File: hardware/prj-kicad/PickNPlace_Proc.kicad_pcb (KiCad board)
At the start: 4 copper layers, 200 x 90 mm, 110 parts, among them J1 Conn_01x09, J10 Conn_01x05, J11 Conn_02x05_Odd_Even, J12 Conn_02x05_Odd_Even, J13 Conn_01x05, J14 Conn_01x03, J15 Conn_01x06, J16 Conn_01x06, J17 Conn_01x12, J2 Conn_01x04, J3 Conn_01x06, J4 Conn_01x04, J5 Conn_01x06, J6 Conn_01x09, J7 Conn_01x02, J8 Conn_01x02, J9 Conn_01x06, Q1 Q_NPN, Q2 Q_NPN, SW1 SW_PUSH, U1 STM32F745ZX, U10 TXS0108E-RGY, U11 TXS0108E-RGY, U2 LM1117-5.0, U3 TPS54160A, U4 TPS54160A, U5 LM1117-5.0, U6 MCP6001T-I_OT, U7 MCP6001T-I_OT, U8 MCP6001T-I_OT, U9 MCP6001T-I_OT

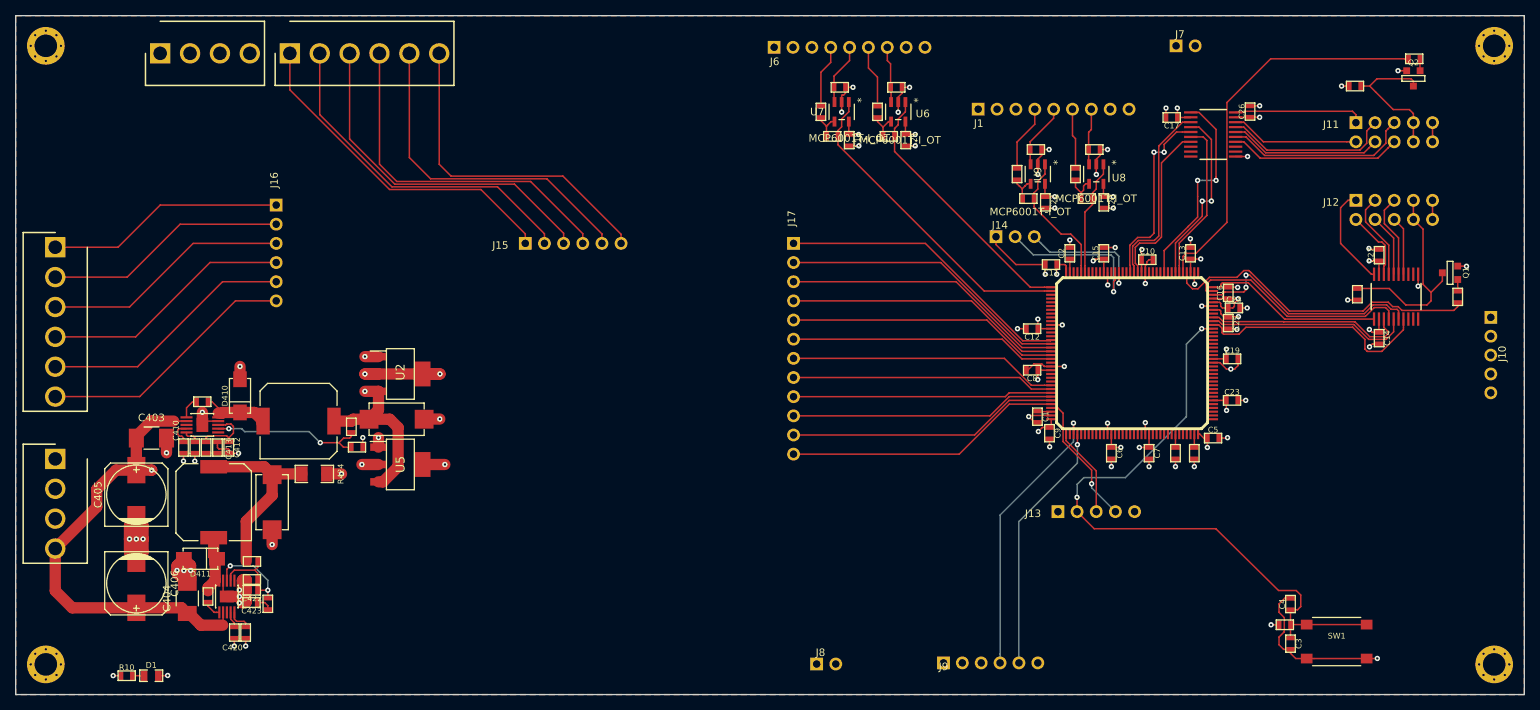
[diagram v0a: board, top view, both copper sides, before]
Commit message: Hardware update (rev2) Pumps, valve, pressure sensors, light, needle + fix enable on lvl shifter
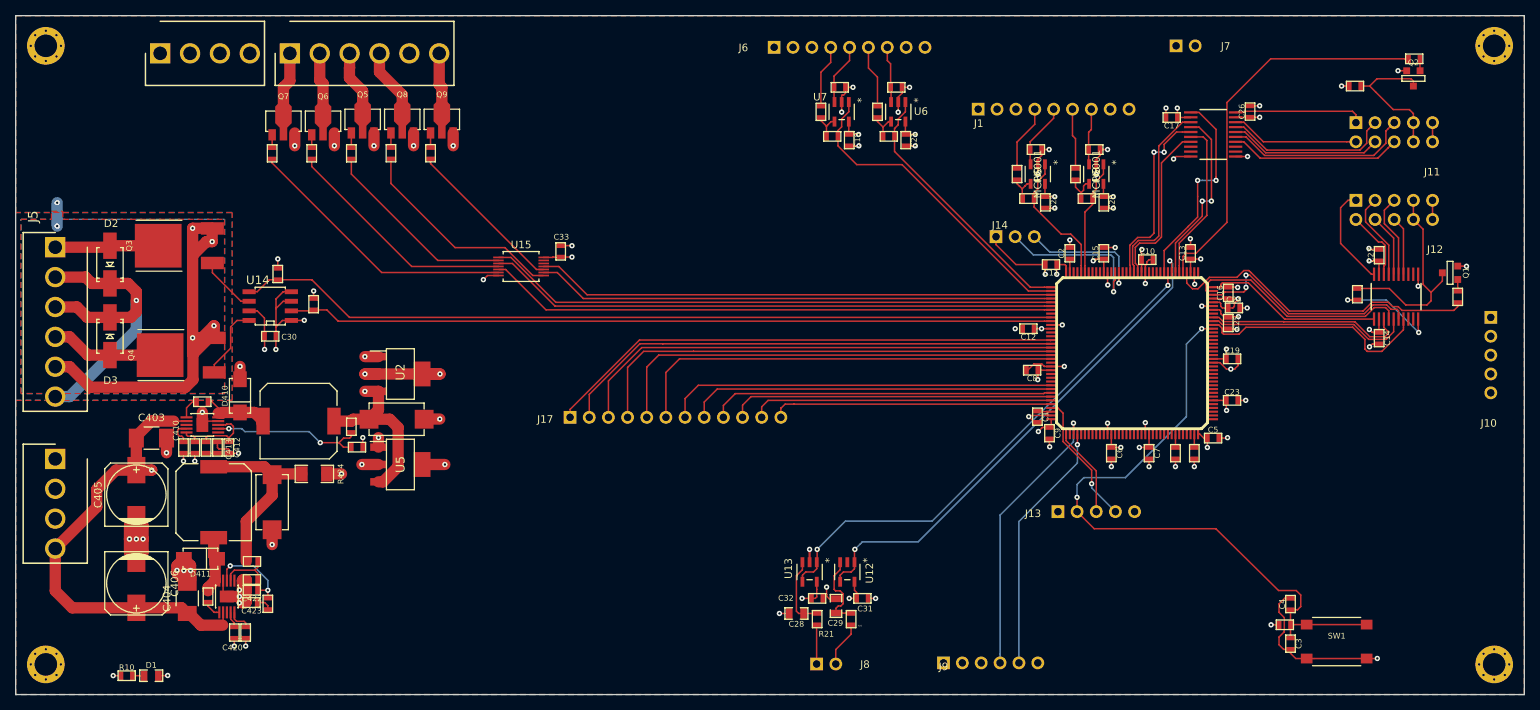
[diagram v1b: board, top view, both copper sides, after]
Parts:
- removed J15, J16: Conn_01x06, PickAndPlace:2_54____6pins
- added C28: 1uF, PickAndPlace:SMD0805, F.Cu at (152.0, 139.2)
- added C29: 1uF, PickAndPlace:SMD0805, F.Cu at (157.2, 138.2)
- added C30: 1uF, PickAndPlace:SMD0603, F.Cu at (82.2, 102.5)
- added C31: 100nF, PickAndPlace:SMD0603, F.Cu at (160.8, 137.2)
- added C32: 100nF, PickAndPlace:SMD0603, F.Cu at (154.8, 137.2)
- added C33: 100nF, PickAndPlace:SMD0603, F.Cu at (120.8, 91.2)
- added D2: S1MLR3, PickAndPlace:D_SMA, F.Cu at (61.0, 93.0)
- added D3: S1MLR3, PickAndPlace:D_SMA, F.Cu at (61.0, 102.5)
- added Q3: Q_NMOS, PickAndPlace:TO-252-2Lead, F.Cu at (67.5, 90.5)
- added Q4: Q_NMOS, PickAndPlace:TO-252-2Lead, F.Cu at (67.8, 105.0)
- added Q5: NPN_2SCR533P_HZG, PickAndPlace:SOT-89, F.Cu at (94.5, 73.8)
- added Q6: NPN_2SCR533P_HZG, PickAndPlace:SOT-89, F.Cu at (89.2, 74.0)
- added Q7: NPN_2SCR533P_HZG, PickAndPlace:SOT-89, F.Cu at (84.0, 74.0)
- added Q8: NPN_2SCR533P_HZG, PickAndPlace:SOT-89, F.Cu at (99.8, 73.8)
- added Q9: NPN_2SCR533P_HZG, PickAndPlace:SOT-89, F.Cu at (105.0, 73.8)
- added R21: 1k, PickAndPlace:R_0603, F.Cu at (154.8, 140.0)
- added R22: 1k, PickAndPlace:R_0603, F.Cu at (159.2, 140.0)
- added R23: 10k, PickAndPlace:R_0603, F.Cu at (83.2, 94.2)
- added R24: 10k, PickAndPlace:R_0603, F.Cu at (88.0, 98.2)
- added R25: 470, PickAndPlace:R_0603, F.Cu at (93.0, 78.2)
- added R26: 470, PickAndPlace:R_0603, F.Cu at (87.8, 78.2)
- added R27: 470, PickAndPlace:R_0603, F.Cu at (82.5, 78.2)
- added R28: 470, PickAndPlace:R_0603, F.Cu at (98.2, 78.2)
- added R29: 470, PickAndPlace:R_0603, F.Cu at (103.5, 78.2)
- added U12: MCP6001, PickAndPlace:MCP6001T-I&slash_OT, F.Cu at (158.8, 133.8)
- added U13: MCP6001, PickAndPlace:MCP6001T-I&slash_OT, F.Cu at (153.8, 133.8)
- added U14: FAN3225TMX, PickAndPlace:SOIC-8, F.Cu at (82.2, 98.5)
- added U15: SN74LVC07ADGVR, PickAndPlace:TVSOP-14_SN74LVC07ADGVR_copy, F.Cu at (115.5, 93.2)
- U6, U7, U8, U9: value MCP6001T-I_OT -> MCP6001
- moved J17 37.5 mm to (122.0, 113.2), turned to 0 degrees
- moved C12 0.50 mm to (182.8, 101.5)
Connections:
- J3 pad 1: OT6 -> Net-(J3-Pad1)
- J3 pad 2: OT5 -> Net-(J3-Pad2)
- J3 pad 3: OT4 -> Net-(J3-Pad3)
- J3 pad 4: OT3 -> Net-(J3-Pad4)
- J3 pad 5: OT2 -> Net-(J3-Pad5)
- J3 pad 6: OT1 -> Net-(J3-Pad6)
- J5 pad 1: PM2 -> Pump_blow-
- J5 pad 2: 24V_1 -> +24V_3
- J5 pad 3: 24V_2 -> +24V_3
- J5 pad 4: PM1 -> Pump_vacuum-
- J5 pad 5: 24v3_1 -> GND
- J5 pad 6: 24v3_2 -> +24V_3
- U1 pad 44: Net-(U1-Pad44) -> RIGHT_NOZZLE_PRESSURE
- U1 pad 45: Net-(U1-Pad45) -> LEFT_NOZZLE_PRESSURE
- U1 pad 75: Net-(U1-Pad75) -> Needle
- U1 pad 76: Net-(U1-Pad76) -> Valve_right
- U1 pad 77: Net-(U1-Pad77) -> Valve_left
- U1 pad 78: Net-(U1-Pad78) -> Downward_light
- U1 pad 79: Net-(U1-Pad79) -> Upward_light
- U1 pad 81: Net-(U1-Pad81) -> BLOW_PWM
- U1 pad 82: Net-(U1-Pad82) -> VACUUM_PWM
- U10 pad 10: Net-(U10-Pad10) -> +3V3
- U11 pad 10: Net-(U11-Pad10) -> +3V3
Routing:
- net BLOW_PWM: track 0.00 -> 109.0 mm
- net VACUUM_PWM: track 0.00 -> 101.4 mm
- net GND: track 182.4 -> 281.1 mm, vias 68 -> 89
- net +3V3: track 415.4 -> 511.5 mm, vias 25 -> 30
- net Valve_left: track 0.00 -> 75.7 mm
- net Downward_light: track 0.00 -> 75.6 mm
- net Upward_light: track 0.00 -> 75.4 mm
- net Needle: track 0.00 -> 68.9 mm
- net Valve_right: track 0.00 -> 68.8 mm
- net LEFT_NOZZLE_PRESSURE: track 0.00 -> 68.4 mm, vias 0 -> 2
- net RIGHT_NOZZLE_PRESSURE: track 0.00 -> 67.6 mm, vias 0 -> 2
- net OT3: track 46.7 -> 0.00 mm
- net OT4: track 46.2 -> 0.00 mm
- net OT5: track 45.7 -> 0.00 mm
- net OT6: track 45.6 -> 0.00 mm
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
